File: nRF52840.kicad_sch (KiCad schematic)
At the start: 19 parts

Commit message: feat(pcb): Version 0.2.1
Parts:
- C10: value (none) -> 4.7uF; footprint (none) -> Capacitor_SMD:C_0402_1005Metric
- C11: value (none) -> 100nF; footprint (none) -> Capacitor_SMD:C_0402_1005Metric
- H1, H2, H3, H4, H5: value (none) -> MountingHole; footprint (none) -> Athena54:MountingHole_4.3mm
- J3: value (none) -> JTAG_TC2030; footprint (none) -> marbastlib-various:CON_TC2030_outlined
- J4: value (none) -> RGB; footprint (none) -> Athena54:LED Header
- L1: value (none) -> NC; footprint (none) -> Inductor_SMD:L_0402_1005Metric
- Q2: value (none) -> 2N7002; footprint (none) -> Package_TO_SOT_SMD:SOT-23
- Q3: value (none) -> AO3407; footprint (none) -> Package_TO_SOT_SMD:SOT-23
- R10: value (none) -> 100R; footprint (none) -> Resistor_SMD:R_0402_1005Metric
- R11, R12: value (none) -> 1K5; footprint (none) -> Resistor_SMD:R_0402_1005Metric
- R13, R14: value (none) -> 10K; footprint (none) -> Resistor_SMD:R_0402_1005Metric
- SW29: value (none) -> RESET; footprint (none) -> Athena54:Panasonic_EVQPUL_EVQPUC (Reversible)
- U4: value (none) -> MS88SF3; footprint (none) -> Athena54:MS88SF3

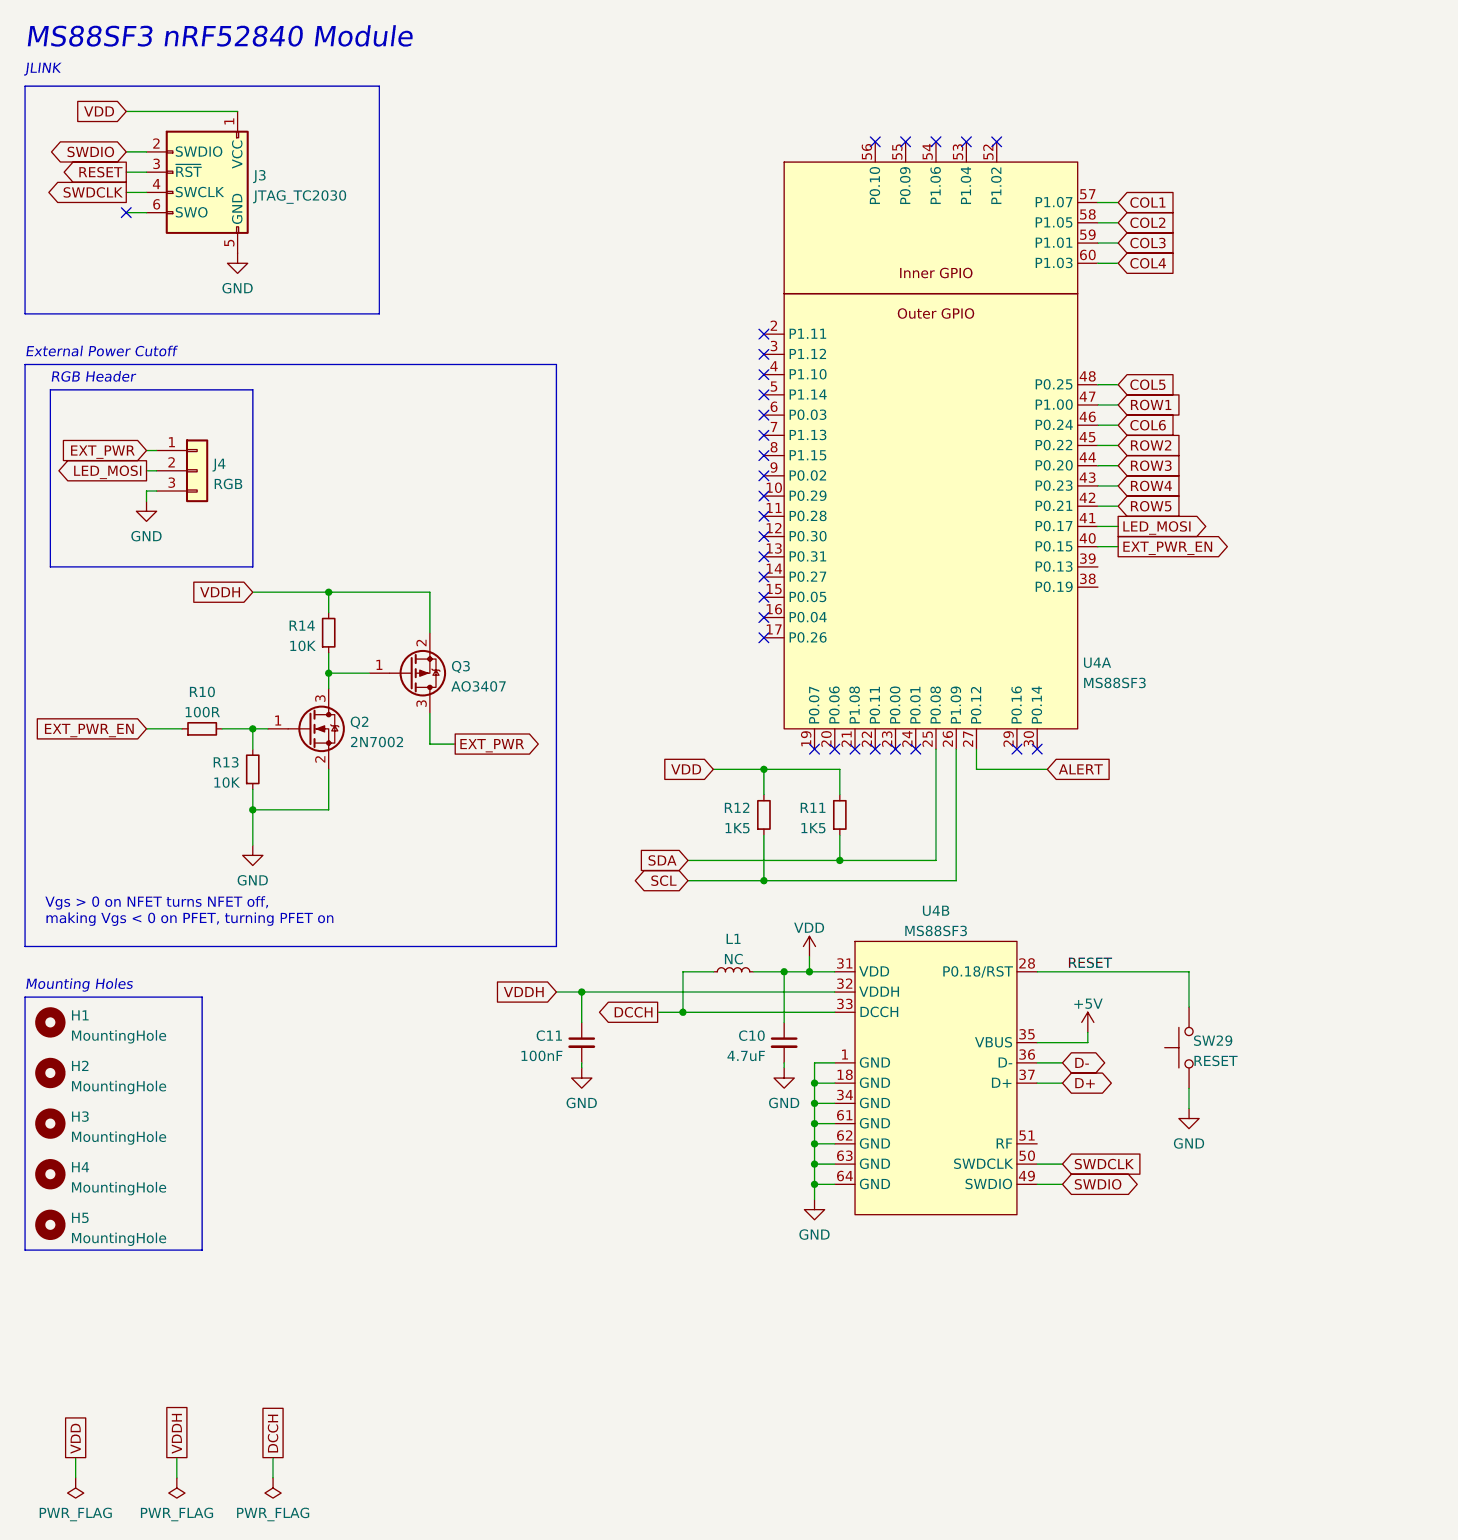
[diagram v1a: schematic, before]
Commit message: fix(schematic): Fix links to footprints
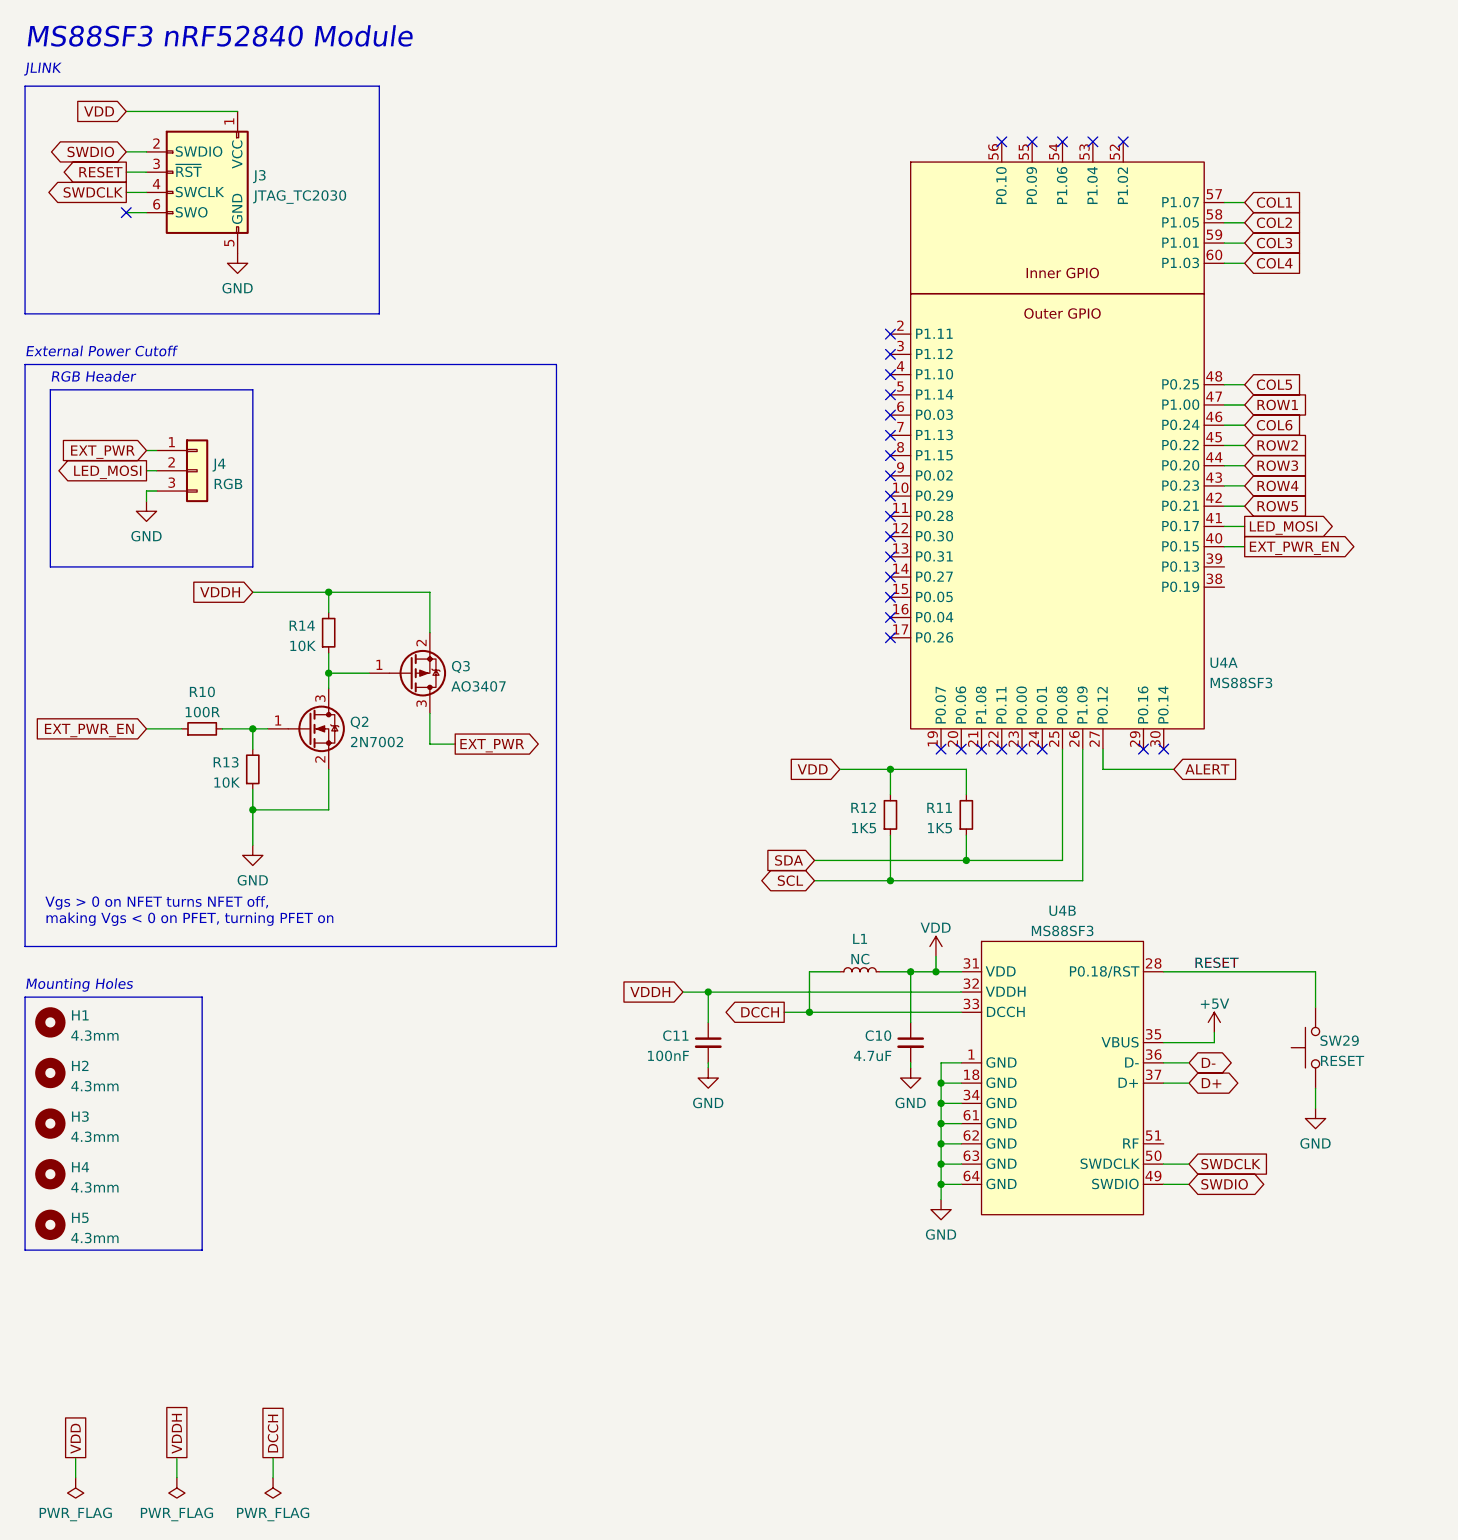
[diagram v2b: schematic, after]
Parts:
- H1, H2, H3, H4, H5: value MountingHole -> 4.3mm
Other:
- moved on the sheet: C10, C11, L1, R11, R12, SW29, U4A, U4B

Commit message: refactor!!!(repository): Rename from Athena54 to Conejo
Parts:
- H1, H2, H3, H4, H5: footprint Athena54:MountingHole_4.3mm -> Conejo:MountingHole_4.3mm
- J4: footprint Athena54:LED Header -> Conejo:LED Header
- SW29: footprint Athena54:Panasonic_EVQPUL_EVQPUC (Reversible) -> Conejo:Panasonic_EVQPUL_EVQPUC (Reversible)
- U4: footprint Athena54:MS88SF3 -> Conejo:MS88SF3
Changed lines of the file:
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@@
       (effects (font (size 1.27 1.27)) (justify left))
     )
-    (property "Footprint" "Athena54:MountingHole_4.3mm" (id 2) (at 15.875 165.1 0)
+    (property "Footprint" "Conejo:MountingHole_4.3mm" (id 2) (at 15.875 165.1 0)
       (effects (font (size 1.27 1.27)) hide)
     )
@@
       (effects (font (size 1.27 1.27)) (justify left))
     )
-    (property "Footprint" "Athena54:LED Header" (id 2) (at 34.29 70.485 0)
+    (property "Footprint" "Conejo:LED Header" (id 2) (at 34.29 70.485 0)
       (effects (font (size 1.27 1.27)) hide)
     )
@@
       (effects (font (size 1.27 1.27)) (justify left))
     )
-    (property "Footprint" "Athena54:MountingHole_4.3mm" (id 2) (at 15.875 146.05 0)
+    (property "Footprint" "Conejo:MountingHole_4.3mm" (id 2) (at 15.875 146.05 0)
       (effects (font (size 1.27 1.27)) hide)
     )
@@
       (effects (font (size 1.27 1.27)) (justify left))
     )
-    (property "Footprint" "Athena54:MountingHole_4.3mm" (id 2) (at 15.875 139.7 0)
+    (property "Footprint" "Conejo:MountingHole_4.3mm" (id 2) (at 15.875 139.7 0)
       (effects (font (size 1.27 1.27)) hide)
     )
@@
       (effects (font (size 1.27 1.27)) (justify left))
     )
-    (property "Footprint" "Athena54:MountingHole_4.3mm" (id 2) (at 15.875 158.75 0)
+    (property "Footprint" "Conejo:MountingHole_4.3mm" (id 2) (at 15.875 158.75 0)
       (effects (font (size 1.27 1.27)) hide)
     )
@@
       (effects (font (size 1.27 1.27)) (justify left))
     )
-    (property "Footprint" "Athena54:MountingHole_4.3mm" (id 2) (at 15.875 152.4 0)
+    (property "Footprint" "Conejo:MountingHole_4.3mm" (id 2) (at 15.875 152.4 0)
       (effects (font (size 1.27 1.27)) hide)
     )
@@
     (property "Reference" "U4" (id 0) (at 142.875 125.7331 0))
     (property "Value" "MS88SF3" (id 1) (at 142.875 128.27 0))
-    (property "Footprint" "Athena54:MS88SF3" (id 2) (at 170.815 171.45 0)
+    (property "Footprint" "Conejo:MS88SF3" (id 2) (at 170.815 171.45 0)
       (effects (font (size 1.27 1.27)) hide)
     )
@@
       (effects (font (size 1.27 1.27)) (justify left))
     )
-    (property "Footprint" "Athena54:MS88SF3" (id 2) (at 170.815 92.71 0)
+    (property "Footprint" "Conejo:MS88SF3" (id 2) (at 170.815 92.71 0)
       (effects (font (size 1.27 1.27)) hide)
     )
@@
       (effects (font (size 1.27 1.27)) (justify right))
     )
-    (property "Footprint" "Athena54:Panasonic_EVQPUL_EVQPUC (Reversible)" (id 2) (at 169.545 142.875 0)
-      (effects (font (size 1.27 1.27)) hide)
-    )
+    (property "Footprint" "Conejo:Panasonic_EVQPUL_EVQPUC (Reversible)" (id 2) (at 169.545 142.875 0)
+      (effects (font (size 1.27 1.27)) hide)
+    )

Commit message: fix(schematic): Further updates to referencing footprints and symbols
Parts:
- U4: symbol Athena54:MS88SF3 -> Conejo:MS88SF3
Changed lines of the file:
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@@
       (effects (font (size 1.27 1.27) italic) (justify left) hide)
     )
-    (property "Datasheet" "http://www.aosmd.com/pdfs/datasheet/AO3407A.pdf" (id 3) (at 60.96 95.885 0)
+    (property "Datasheet" "http://www.aosmd.com/pdfs/datasheet/AO3401A.pdf" (id 3) (at 60.96 95.885 0)
       (effects (font (size 1.27 1.27)) (justify left) hide)
     )
@@
     (pin "1")
   )
-  (symbol (lib_id "Athena54:MS88SF3") (at 142.875 147.32 0) (unit 2)
+  (symbol (lib_id "Conejo:MS88SF3") (at 142.875 147.32 0) (unit 2)
     (in_bom yes) (on_board yes)
     (property "Reference" "U4" (id 0) (at 142.875 125.7331 0))
     (property "Value" "MS88SF3" (id 1) (at 142.875 128.27 0))
-    (property "Footprint" "Conejo:MS88SF3" (id 2) (at 170.815 171.45 0)
-      (effects (font (size 1.27 1.27)) hide)
-    )
-    (property "Datasheet" "" (id 3) (at 146.685 114.3 0)
+    (property "Footprint" "Conejo:MS88SF3" (id 2) (at 170.815 179.07 0)
+      (effects (font (size 1.27 1.27)) hide)
+    )
+    (property "Datasheet" "" (id 3) (at 146.685 93.98 0)
       (effects (font (size 1.27 1.27)) hide)
     )
@@
     (pin "6")
   )
-  (symbol (lib_id "Athena54:MS88SF3") (at 142.875 68.58 0) (unit 1)
+  (symbol (lib_id "Conejo:MS88SF3") (at 142.875 68.58 0) (unit 1)
     (in_bom yes) (on_board yes)
     (property "Reference" "U4" (id 0) (at 161.29 94.615 0)
@@
       (effects (font (size 1.27 1.27)) (justify left))
     )
-    (property "Footprint" "Conejo:MS88SF3" (id 2) (at 170.815 92.71 0)
-      (effects (font (size 1.27 1.27)) hide)
-    )
-    (property "Datasheet" "" (id 3) (at 146.685 35.56 0)
+    (property "Footprint" "Conejo:MS88SF3" (id 2) (at 170.815 100.33 0)
+      (effects (font (size 1.27 1.27)) hide)
+    )
+    (property "Datasheet" "" (id 3) (at 146.685 15.24 0)
       (effects (font (size 1.27 1.27)) hide)
     )
@@
       (effects (font (size 1.27 1.27) italic) (justify left) hide)
     )
-    (property "Datasheet" "" (id 3) (at 48.26 102.87 0)
+    (property "Datasheet" "http://www.aosmd.com/pdfs/datasheet/AO3400A.pdf" (id 3) (at 48.26 102.87 0)
       (effects (font (size 1.27 1.27)) (justify left) hide)
     )
